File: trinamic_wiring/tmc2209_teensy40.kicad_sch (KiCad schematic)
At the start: 4 parts, among them M1 Stepper_Motor_QSH2818-32-07-0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

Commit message: Add text to schematic
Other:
- note added: "Must solder jumper pads on the SilentStepStick to connect both the UART and PDN pins to the PDN_UART line on the chip!"
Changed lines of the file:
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@@
     (stroke (width 0) (type default) (color 0 0 0 0))
+  )
+  (text "Must solder jumper pads on the SilentStepStick\nto connect both the UART and PDN pins to the\nPDN_UART line on the chip!"
+    (at 132.08 127 0)
+    (effects (font (size 1.27 1.27)) (justify left bottom))
   )
   (label "A" (at 194.31 96.52 180)

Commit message: Modify wiring
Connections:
- net ~{ENABLE}: now also SS1.7 (GND); no longer TEENSY1.4 (D4/BCLK2/PWM)
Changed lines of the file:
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@@
   (no_connect (at 137.16 109.22))
   (no_connect (at 137.16 104.14))
-  (no_connect (at 153.67 116.84))
+  (no_connect (at 52.07 93.98))
   (no_connect (at 137.16 93.98))
   (wire (pts (xy 115.57 81.28) (xy 118.11 81.28))
@@
     (stroke (width 0) (type default) (color 0 0 0 0))
   )
-  (wire (pts (xy 52.07 93.98) (xy 49.53 93.98))
+  (wire (pts (xy 153.67 116.84) (xy 153.67 119.38))
     (stroke (width 0) (type default) (color 0 0 0 0))
   )
@@
     (stroke (width 0) (type default) (color 0 0 0 0))
   )
+  (wire (pts (xy 153.67 119.38) (xy 156.21 119.38))
+    (stroke (width 0) (type default) (color 0 0 0 0))
+  )
   (wire (pts (xy 134.62 96.52) (xy 137.16 96.52))
     (stroke (width 0) (type default) (color 0 0 0 0))
@@
     (effects (font (size 1.27 1.27)) (justify right bottom))
   )
-  (label "~{ENABLE}" (at 49.53 93.98 180)
-    (effects (font (size 1.27 1.27)) (justify right bottom))
+  (label "~{ENABLE}" (at 156.21 119.38 0)
+    (effects (font (size 1.27 1.27)) (justify left bottom))
   )
   (label "A" (at 170.18 95.25 0)

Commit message: Update version
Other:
- company: (none) -> Janelia Research Campus
- title: TMC2209 TEENSY4.0 -> Trinamic Wiring

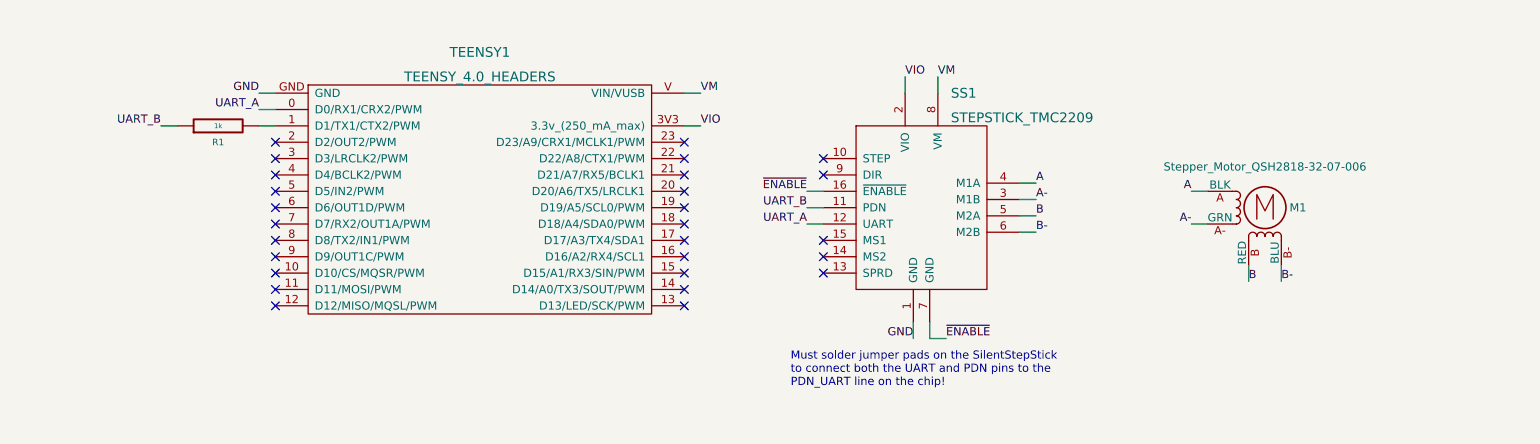
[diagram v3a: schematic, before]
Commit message: Make updates for new version of TMC2209 library
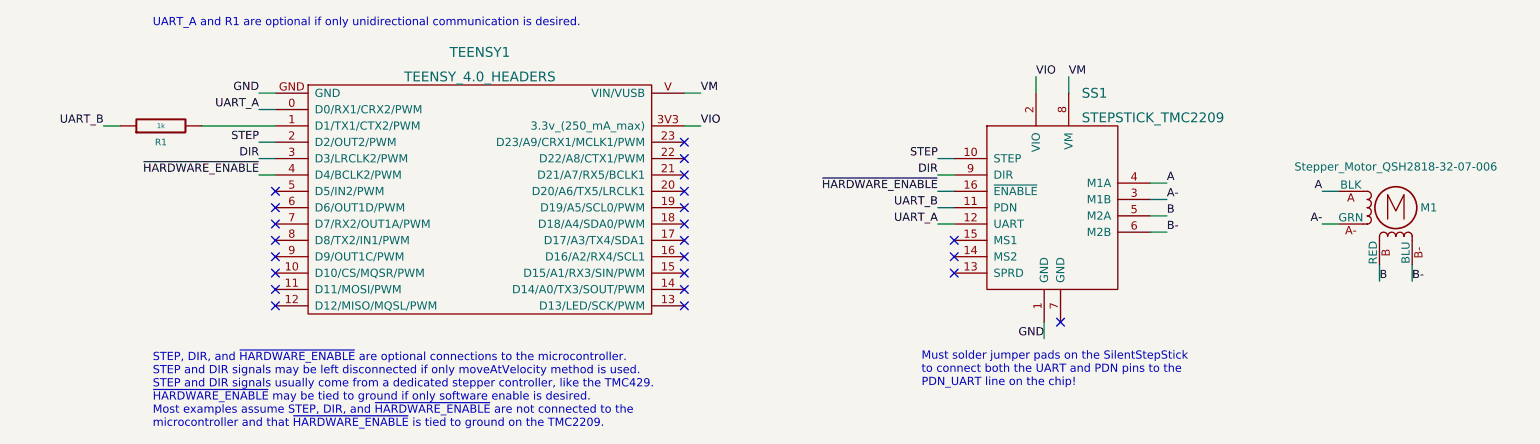
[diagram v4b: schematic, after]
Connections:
- net STEP: now reaches SS1.10 (STEP)
- net STEP: now also TEENSY1.2 (D2/OUT2/PWM)
- net DIR: now reaches SS1.9 (DIR)
- net DIR: now also TEENSY1.3 (D3/LRCLK2/PWM)
- net ~{HARDWARE_ENABLE}: now reaches TEENSY1.4 (D4/BCLK2/PWM)
- net ~{HARDWARE_ENABLE}: now also SS1.16 (~{ENABLE})
- net ~{ENABLE}: no longer names the net of SS1.7 (GND)
- net ~{ENABLE}: no longer SS1.16 (~{ENABLE})
- no-connect marks 27 -> 23
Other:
- note added: "STEP, DIR, and ~{HARDWARE_ENABLE} are optional connections to the microcontroller. STEP and DIR signals may be left disconnected if only moveAtVelocity method is used. STEP and DIR signals usually come from a dedicated stepper controller, like the TMC429. ~{HARDWARE_ENABLE} may be tied to ground if only software enable is desired. Most examples assume STEP, DIR, and ~{HARDWARE_ENABLE} are not con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"
- note added: "UART_A and R1 are optional if only unidirectional communication is desired."
- moved on the sheet: M1, R1, SS1

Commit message: Update wiring for TMC2209 v9
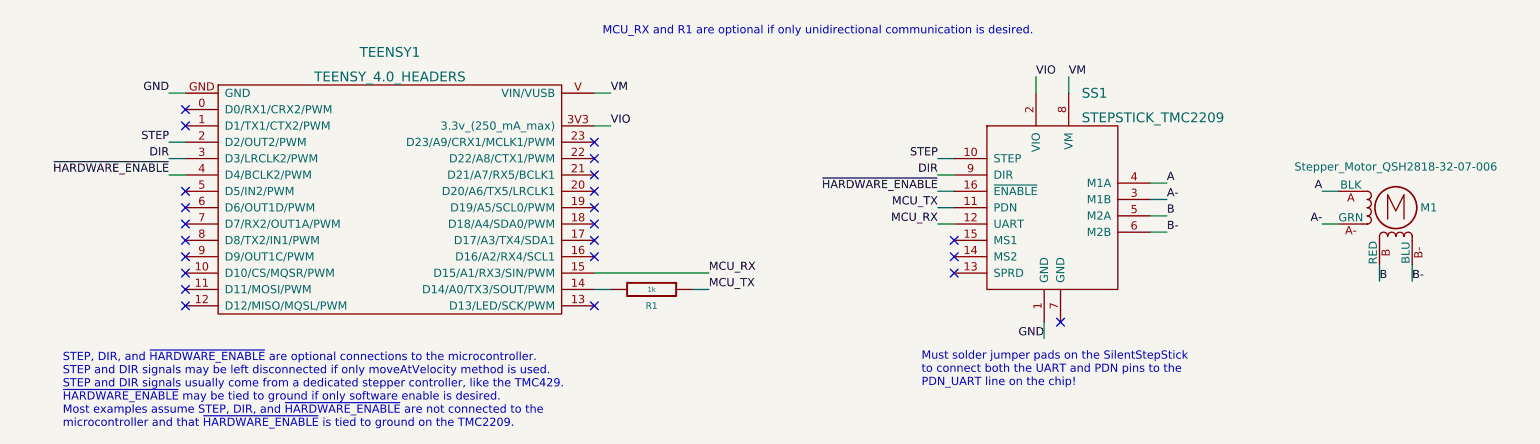
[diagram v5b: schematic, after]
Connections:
- net at TEENSY1.1 (D1/TX1/CTX2/PWM): no longer R1.2
- net at TEENSY1.14 (D14/A0/TX3/SOUT/PWM): now also R1.2
- net MCU_RX: now reaches TEENSY1.15 (D15/A1/RX3/SIN/PWM)
- net MCU_RX: now also SS1.12 (UART)
- net UART_A: no longer names the net of TEENSY1.0 (D0/RX1/CRX2/PWM)
- net UART_A: no longer SS1.12 (UART)
- net UART_B renamed MCU_TX
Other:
- note added: "MCU_RX and R1 are optional if only unidirectional communication is desired."
- note removed: "UART_A and R1 are optional if only unidirectional communication is desired."
- moved on the sheet: R1, TEENSY1

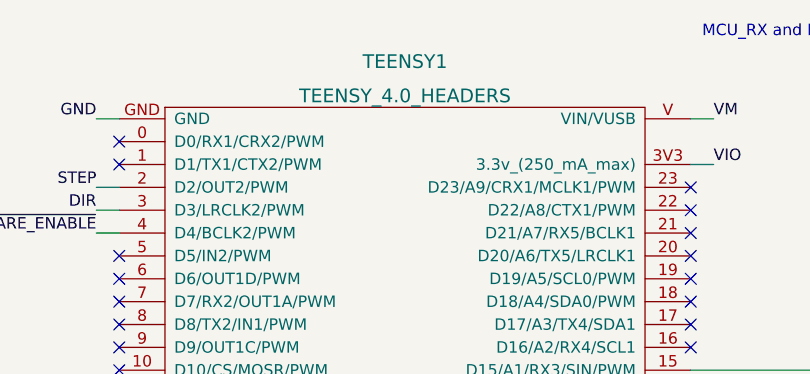
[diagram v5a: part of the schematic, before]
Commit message: Add uno
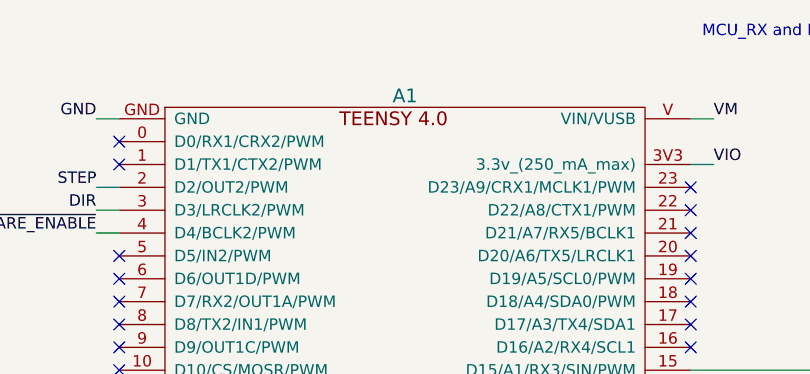
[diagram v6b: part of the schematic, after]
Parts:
- A1: renamed from TEENSY1; footprint footprints:TEENSY_4.0_HEADERS -> Janelia:TEENSY_4.0_HEADERS; Quantity 2 -> (none)
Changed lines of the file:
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@@
   (title_block
     (title "Trinamic Wiring")
-    (date "2023-04-27")
+    (date "2023-06-27")
     (rev "0.3")
     (company "Janelia Research Campus")
@@
   (symbol (lib_id "Janelia:TEENSY_4.0_HEADERS") (at 69.85 97.79 0) (unit 1)
     (in_bom yes) (on_board yes) (dnp no) (fields_autoplaced)
-    (property "Reference" "TEENSY1" (at 69.85 74.93 0)
+    (property "Reference" "A1" (at 69.85 78.74 0) (do_not_autoplace)
       (effects (font (size 1.524 1.524)))
     )
-    (property "Value" "TEENSY_4.0_HEADERS" (at 69.85 78.74 0)
-      (effects (font (size 1.524 1.524)))
-    )
-    (property "Footprint" "footprints:TEENSY_4.0_HEADERS" (at 69.85 71.12 0)
+    (property "Value" "TEENSY_4.0_HEADERS" (at 69.85 116.84 0) (do_not_autoplace)
+      (effects (font (size 1.524 1.524)) hide)
+    )
+    (property "Footprint" "Janelia:TEENSY_4.0_HEADERS" (at 69.85 71.12 0)
       (effects (font (size 1.524 1.524)) hide)
     )
@@
       (effects (font (size 1.524 1.524)) hide)
     )
-    (property "Quantity" "2" (at 69.85 97.79 0)
-      (effects (font (size 1.27 1.27)) hide)
-    )
     (property "Manufacturer" "Sullins Connector Solutions" (at 69.85 97.79 0)
       (effects (font (size 1.27 1.27)) hide)
     )
     (property "Manufacturer Part Number" "PPPC141LFBN-RC" (at 69.85 97.79 0)
+      (effects (font (size 1.27 1.27)) hide)
+    )
+    (property "Sim.Enable" "0" (at 69.85 97.79 0)
       (effects (font (size 1.27 1.27)) hide)
     )
@@
       (project "trinamic_wiring"
         (path "/e4144788-6304-493f-818e-5d881d3b7418/c8eda2b5-ab13-4033-82d9-875c9fcaf884/2a1dc514-7df6-499f-97d3-aee7548517ec"
-          (reference "TEENSY1") (unit 1)
+          (reference "A1") (unit 1)
         )
       )
